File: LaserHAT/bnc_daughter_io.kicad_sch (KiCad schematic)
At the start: 11 parts, among them J6 SMA TRIGGER IN, J7 SMA STIM OUT, J8 DB_POWER_TIMING, J9 DB_ANALOG, U8 74LVC2G17

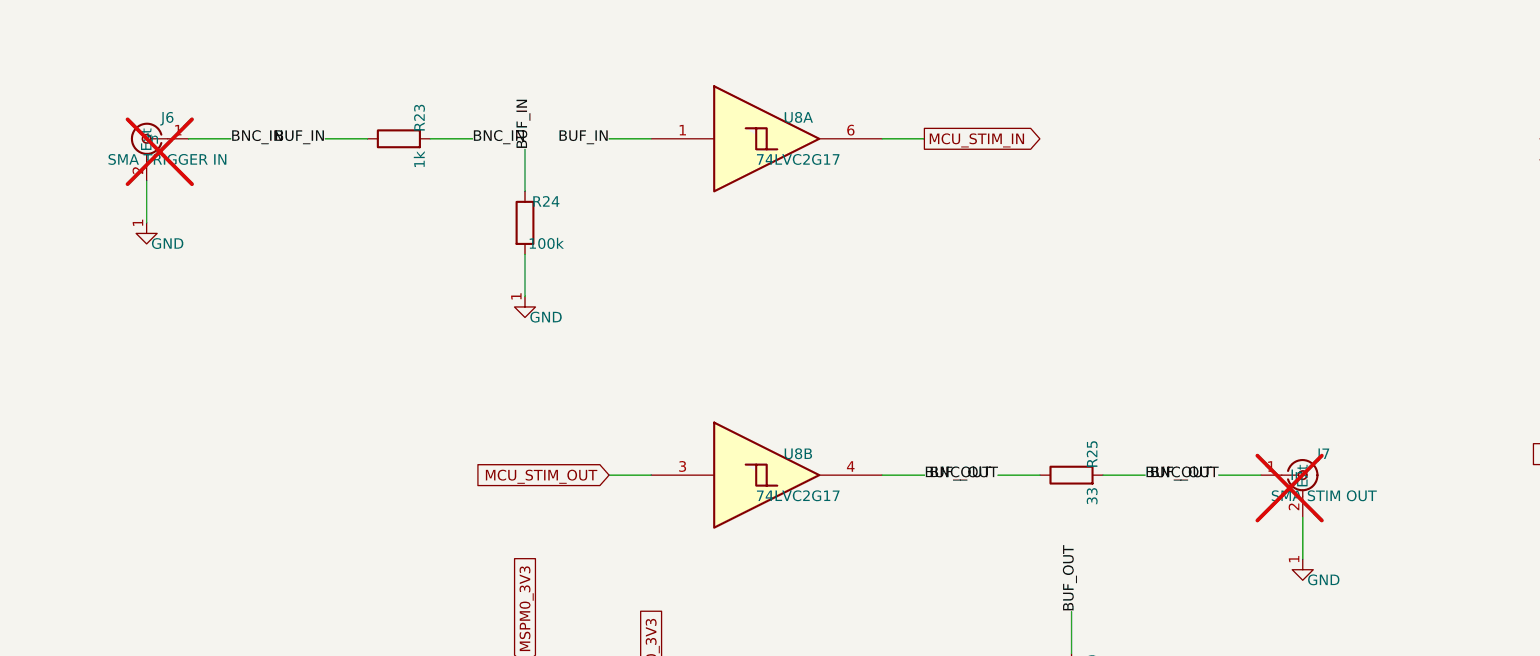
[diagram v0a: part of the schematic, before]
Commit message: Revert "LaserHAT: J6/J7 become right-angle SMA jacks (Amphenol 901-143) in the schematic"
This reverts commit b6c5e68: the BNCs stay. The e-stim module will instead extend
12.5 mm south over the Pi's port edge (26.5 x 36.5 mm), which routes single-sided.
The study file is kept, with a note that it is superseded.

Co-Authored-By: Claude Fable 5.1 <noreply@anthropic.com>
Claude-Session: https://claude.ai/code/session_018vgLizGzYPynnY93ajvoVA
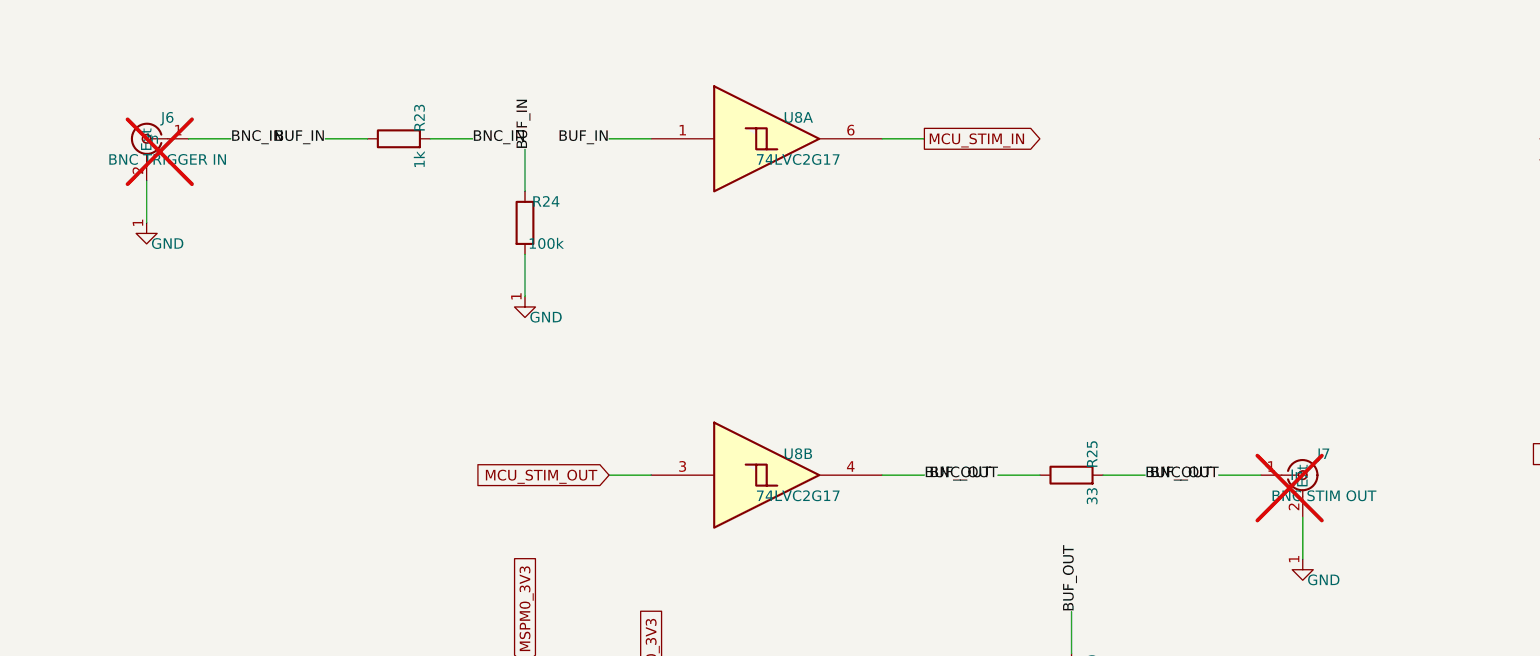
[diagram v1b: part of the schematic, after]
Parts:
- J6: value SMA TRIGGER IN -> BNC TRIGGER IN; footprint Footprints:SMA_Amphenol_901-143_Horizontal -> Footprints:BNC_Amphenol_031-5540_031-5539_Dual
- J7: value SMA STIM OUT -> BNC STIM OUT; footprint Footprints:SMA_Amphenol_901-143_Horizontal -> Footprints:BNC_Amphenol_031-5540_031-5539_Dual
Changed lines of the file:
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@@
       (effects (font (size 1.27 1.27)))
     )
-    (property "Value" "SMA TRIGGER IN" (id 1) (at 48.26 63.5 0)
+    (property "Value" "BNC TRIGGER IN" (id 1) (at 48.26 63.5 0)
       (effects (font (size 1.27 1.27)))
     )
-    (property "Footprint" "Footprints:SMA_Amphenol_901-143_Horizontal" (id 2) (at 45.72 60.96 0)
+    (property "Footprint" "Footprints:BNC_Amphenol_031-5540_031-5539_Dual" (id 2) (at 45.72 60.96 0)
       (effects (font (size 1.27 1.27)) hide)
     )
@@
       (effects (font (size 1.27 1.27)))
     )
-    (property "Value" "SMA STIM OUT" (id 1) (at 187.96 104.14 0)
+    (property "Value" "BNC STIM OUT" (id 1) (at 187.96 104.14 0)
       (effects (font (size 1.27 1.27)))
     )
-    (property "Footprint" "Footprints:SMA_Amphenol_901-143_Horizontal" (id 2) (at 185.42 101.6 0)
+    (property "Footprint" "Footprints:BNC_Amphenol_031-5540_031-5539_Dual" (id 2) (at 185.42 101.6 0)
       (effects (font (size 1.27 1.27)) hide)
     )

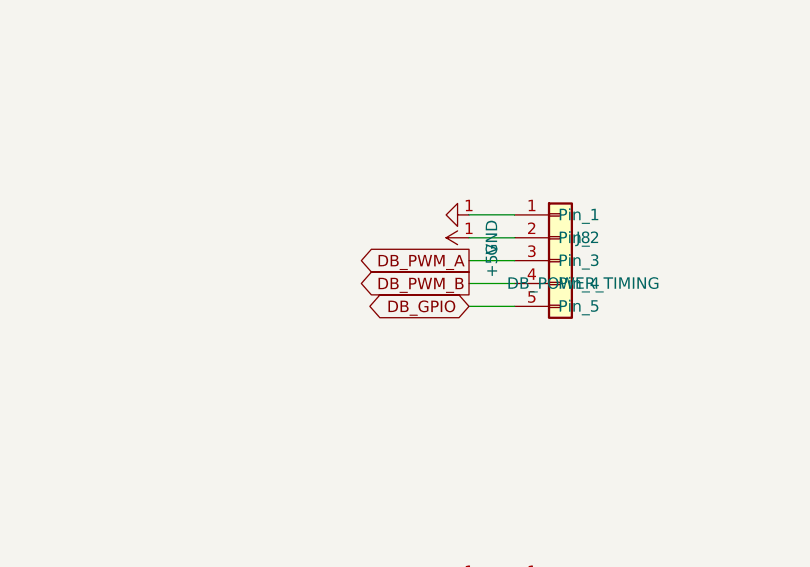
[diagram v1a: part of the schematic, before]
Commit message: LaserHAT: J8.3 = FAULT_n (PA6), J8.5 = EN/PWM_A (PA7) on the HAT and the laser module
Follows the e-stim module's connector standard (spec §3/§7, LAYOUT_HANDOFF Q2):
- bnc_daughter_io.kicad_sch: DB_GPIO on J8.3, DB_PWM_A on J8.5 (rev2_migrate.py matches)
- LaserDriver.kicad_pcb: J8 pads re-netted, PA6/PA7 traces re-routed along the old
  corridors (same vias at U7); DRC unchanged, 0 unconnected; backup in stash/
- LaserDaughter: J1.5 = DB_PWM_A, J1.3 n/c; schematic regenerated, board re-routed
- REV2_NOTES/CLAUDE.md: PA17/PA22 rows now say I2C SDA/SCL; note on why hardware I2C1
  cannot use them and the re-map that would (J9.4 -> PA16, J9.5 -> PA17, BUTTON3 -> PA22)
- LAYOUT_HANDOFF Q1/Q2 answered, spec §7 marked applied, fab outputs regenerated
- tools/schlib.py: symbol dir from env / Linux default

Co-Authored-By: Claude Fable 5.1 <noreply@anthropic.com>
Claude-Session: https://claude.ai/code/session_018vgLizGzYPynnY93ajvoVA
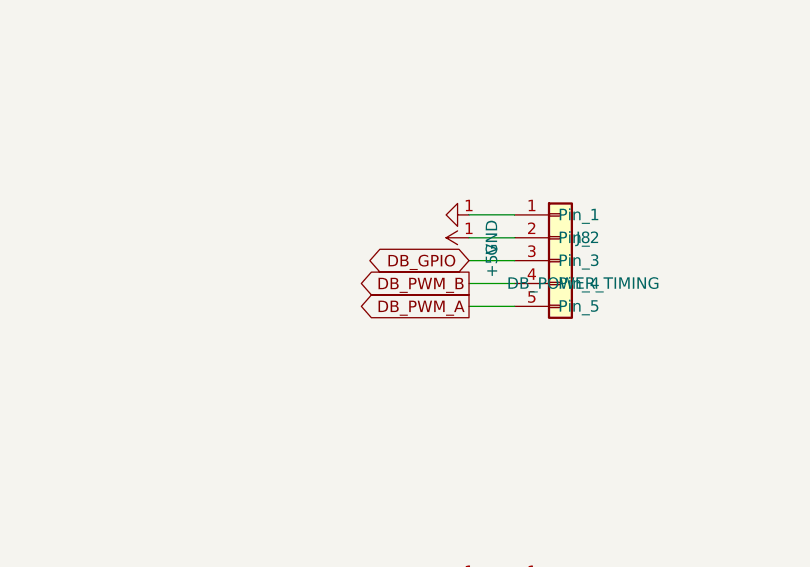
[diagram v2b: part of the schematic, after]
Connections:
- net DB_GPIO: now also J8.3 (Pin_3); no longer J8.5 (Pin_5)
- net DB_PWM_A: now also J8.5 (Pin_5); no longer J8.3 (Pin_3)
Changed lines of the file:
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@@
     )
   )
-  (global_label "DB_PWM_A" (shape output) (at 226.06 60.96 180) (fields_autoplaced)
+  (global_label "DB_GPIO" (shape bidirectional) (at 226.06 60.96 180) (fields_autoplaced)
     (effects (font (size 1.27 1.27)) (justify right))
     (property "Intersheetrefs" "${INTERSHEET_REFS}" (id 0) (at 226.06 60.96 0)
@@
     )
   )
-  (global_label "DB_GPIO" (shape bidirectional) (at 226.06 66.04 180) (fields_autoplaced)
+  (global_label "DB_PWM_A" (shape output) (at 226.06 66.04 180) (fields_autoplaced)
     (effects (font (size 1.27 1.27)) (justify right))
     (property "Intersheetrefs" "${INTERSHEET_REFS}" (id 0) (at 226.06 66.04 0)
